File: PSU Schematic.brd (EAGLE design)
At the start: 50 x 100 mm, 19 parts, among them IC1 LM34, J1 POWERPOLE_POWER45A, J2 FUSEATC, J3 POWERPOLE_POWER45A, J4 FUSEATC

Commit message: Layout revision
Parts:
- removed U$2: SINGLE, con-lstb:SINGLE
- added CS: SINGLE, con-lstb:SINGLE
- moved IC1 2.00 mm to (14.1, 20.7)
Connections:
- net CURRENTSHARE: now also CS.1; no longer U$2.1
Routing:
- net CURRENTSHARE: track 26.0 -> 39.3 mm
- net LVCC: track 15.3 -> 18.2 mm, vias 30 -> 33
- net FAN: track 27.1 -> 29.1 mm
- net GND: track 23.1 -> 25.0 mm
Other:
- board text added: "FAN"
- board text added: "VCC"
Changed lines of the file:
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@@
 <vertex x="34.5" y="51"/>
 </polygon>
+<text x="23.5" y="29" size="1.778" layer="25" rot="R90">FAN</text>
+<text x="18" y="23" size="1.778" layer="25" rot="R270">VCC</text>
 </plain>
 <attributes>
@@
 </element>
 <element name="C2" library="resistor" package="C050-025X075" value="" x="44.09" y="81.37" rot="R270"/>
-<element name="IC1" library="linear" package="TO92" value="LM34" x="16.1" y="20.68" smashed="yes" rot="R180">
-<attribute name="NAME" x="17.687" y="24.029" size="1.27" layer="25" ratio="10" rot="R180"/>
+<element name="IC1" library="linear" package="TO92" value="LM34" x="14.1" y="20.68" smashed="yes" rot="R180">
+<attribute name="NAME" x="15.687" y="24.029" size="1.27" layer="25" ratio="10" rot="R180"/>
 </element>
 <element name="H4" library="holes" package="4,1-PAD" value="MOUNT-PAD-ROUND4.1" x="5" y="95"/>
@@
 <attribute name="NAME" x="20.428" y="23.167" size="1.27" layer="25" ratio="10"/>
 </element>
-<element name="U$2" library="con-lstb" package="SINGLE" value="SINGLE" x="13" y="20.5" smashed="yes">
-<attribute name="NAME" x="9.19" y="22.151" size="1.27" layer="25" ratio="10"/>
+<element name="CS" library="con-lstb" package="SINGLE" value="SINGLE" x="13" y="31" smashed="yes">
+<attribute name="NAME" x="9.19" y="27.651" size="1.27" layer="25" ratio="10"/>
 </element>
-<element name="R3" library="pot" package="RJ9W" value="T93YA" x="26.5" y="29.5" rot="R90"/>
+<element name="R3" library="pot" package="RJ9W" value="T93YA" x="26.5" y="29.5" smashed="yes" rot="R90">
+<attribute name="NAME" x="23.833" y="24.928" size="1.27" layer="25" ratio="10" rot="R90"/>
+</element>
 </elements>
 <signals>
@@
 <via x="16" y="48" extent="1-16" drill="0.6"/>
 <contactref element="R3" pad="E"/>
-<wire x1="23.5" y1="26.875" x2="17.375" y2="20.75" width="0.127" layer="1"/>
-<wire x1="25.75" y1="26.875" x2="23.5" y2="26.875" width="0.127" layer="1"/>
-<wire x1="17.375" y1="20.75" x2="17.37" y2="20.68" width="0.127" layer="1"/>
+<wire x1="25.75" y1="26.875" x2="23.622" y2="26.875" width="0.127" layer="1"/>
+<wire x1="23.622" y1="26.875" x2="23.5" y2="26.875" width="0.127" layer="1"/>
 <wire x1="25.75" y1="26.875" x2="25.865" y2="26.96" width="0.127" layer="1"/>
 <wire x1="30" y1="27" x2="25.875" y2="27" width="0.127" layer="1"/>
 <wire x1="25.875" y1="27" x2="25.865" y2="26.96" width="0.127" layer="1"/>
+<wire x1="15.4305" y1="22.098" x2="15.4305" y2="20.7645" width="0.127" layer="1"/>
+<wire x1="20.193" y1="26.8605" x2="15.4305" y2="22.098" width="0.127" layer="1"/>
+<wire x1="23.622" y1="26.8605" x2="20.193" y2="26.8605" width="0.127" layer="1"/>
+<wire x1="15.4305" y1="20.7645" x2="15.37" y2="20.68" width="0.127" layer="1"/>
+<wire x1="23.622" y1="26.8605" x2="23.622" y2="26.875" width="0.127" layer="1"/>
+<via x="46" y="33" extent="1-16" drill="0.6"/>
+<via x="46" y="43" extent="1-16" drill="0.6"/>
+<via x="46" y="38" extent="1-16" drill="0.6"/>
 </signal>
 <signal name="FAN">
@@
 <contactref element="U$1" pad="SIG4"/>
 <contactref element="R3" pad="S"/>
-<wire x1="21.375" y1="18.75" x2="16.125" y2="18.75" width="0.127" layer="16"/>
-<wire x1="21.375" y1="11.375" x2="21.375" y2="18.75" width="0.127" layer="16"/>
+<wire x1="21.375" y1="11.375" x2="21.375" y2="18.8595" width="0.127" layer="16"/>
+<wire x1="21.375" y1="18.8595" x2="21.375" y2="25.125" width="0.127" layer="16"/>
 <wire x1="22.5" y1="10.25" x2="21.375" y2="11.375" width="0.127" layer="16"/>
-<wire x1="16.125" y1="18.75" x2="16.1" y2="18.775" width="0.127" layer="16"/>
 <wire x1="22.5" y1="10.25" x2="22.61" y2="10.16" width="0.127" layer="16"/>
 <wire x1="21.375" y1="25.125" x2="25.75" y2="29.5" width="0.127" layer="16"/>
-<wire x1="21.375" y1="18.75" x2="21.375" y2="25.125" width="0.127" layer="16"/>
 <wire x1="25.75" y1="29.5" x2="25.865" y2="29.5" width="0.127" layer="16"/>
+<wire x1="21.375" y1="18.8595" x2="14.2875" y2="18.8595" width="0.127" layer="16"/>
+<wire x1="14.2875" y1="18.8595" x2="14.1" y2="18.775" width="0.127" layer="16"/>
 </signal>
 <signal name="GND">
@@
 <contactref element="IC1" pad="3"/>
 <contactref element="R3" pad="A"/>
-<wire x1="14.875" y1="16.5" x2="14.875" y2="20.625" width="0.127" layer="16"/>
-<wire x1="14.875" y1="20.625" x2="14.83" y2="20.68" width="0.127" layer="16"/>
-<wire x1="14.875" y1="21.125" x2="25.75" y2="32" width="0.127" layer="16"/>
-<wire x1="14.875" y1="20.75" x2="14.875" y2="21.125" width="0.127" layer="16"/>
 <wire x1="25.75" y1="32" x2="25.865" y2="32.04" width="0.127" layer="16"/>
-<wire x1="14.875" y1="20.75" x2="14.83" y2="20.68" width="0.127" layer="16"/>
+<wire x1="12.7635" y1="16.5" x2="12.7635" y2="20.574" width="0.127" layer="1"/>
+<wire x1="12.7635" y1="20.574" x2="12.83" y2="20.68" width="0.127" layer="1"/>
+<wire x1="24.1935" y1="32.004" x2="25.7175" y2="32.004" width="0.127" layer="16"/>
+<wire x1="12.954" y1="20.7645" x2="24.1935" y2="32.004" width="0.127" layer="16"/>
+<wire x1="25.7175" y1="32.004" x2="25.865" y2="32.04" width="0.127" layer="16"/>
+<wire x1="12.954" y1="20.7645" x2="12.83" y2="20.68" width="0.127" layer="16"/>
 </signal>
 <signal name="CURRENTSHARE">
 <contactref element="U$1" pad="SIG11"/>
-<contactref element="U$2" pad="1"/>
-<wire x1="13.875" y1="17.125" x2="10.5" y2="20.5" width="0.127" layer="1"/>
-<wire x1="20.375" y1="17.125" x2="13.875" y2="17.125" width="0.127" layer="1"/>
-<wire x1="24" y1="13.5" x2="20.375" y2="17.125" width="0.127" layer="1"/>
-<wire x1="24" y1="5.125" x2="24" y2="13.5" width="0.127" layer="1"/>
-<wire x1="25.125" y1="5.125" x2="24" y2="5.125" width="0.127" layer="1"/>
-<wire x1="10.5" y1="20.5" x2="10.46" y2="20.5" width="0.127" layer="1"/>
-<wire x1="25.125" y1="5.125" x2="25.15" y2="5.08" width="0.127" layer="1"/>
-</signal>
-<signal name="LVCC1">
-<via x="46" y="33" extent="1-16" drill="0.6"/>
-<via x="46" y="43" extent="1-16" drill="0.6"/>
-<via x="46" y="38" extent="1-16" drill="0.6"/>
+<contactref element="CS" pad="1"/>
+<wire x1="10.4775" y1="20.955" x2="10.4775" y2="30.861" width="0.127" layer="16"/>
+<wire x1="14.2875" y1="17.145" x2="10.4775" y2="20.955" width="0.127" layer="16"/>
+<wire x1="20.193" y1="17.145" x2="14.2875" y2="17.145" width="0.127" layer="16"/>
+<wire x1="20.955" y1="16.383" x2="20.193" y2="17.145" width="0.127" layer="16"/>
+<wire x1="20.955" y1="4.572" x2="20.955" y2="16.383" width="0.127" layer="16"/>
+<wire x1="21.717" y1="3.81" x2="20.955" y2="4.572" width="0.127" layer="16"/>
+<wire x1="24.003" y1="3.81" x2="21.717" y2="3.81" width="0.127" layer="16"/>
+<wire x1="25.146" y1="4.953" x2="24.003" y2="3.81" width="0.127" layer="16"/>
+<wire x1="10.4775" y1="30.861" x2="10.46" y2="31" width="0.127" layer="16"/>
+<wire x1="25.146" y1="4.953" x2="25.15" y2="5.08" width="0.127" layer="16"/>
 </signal>
 </signals>

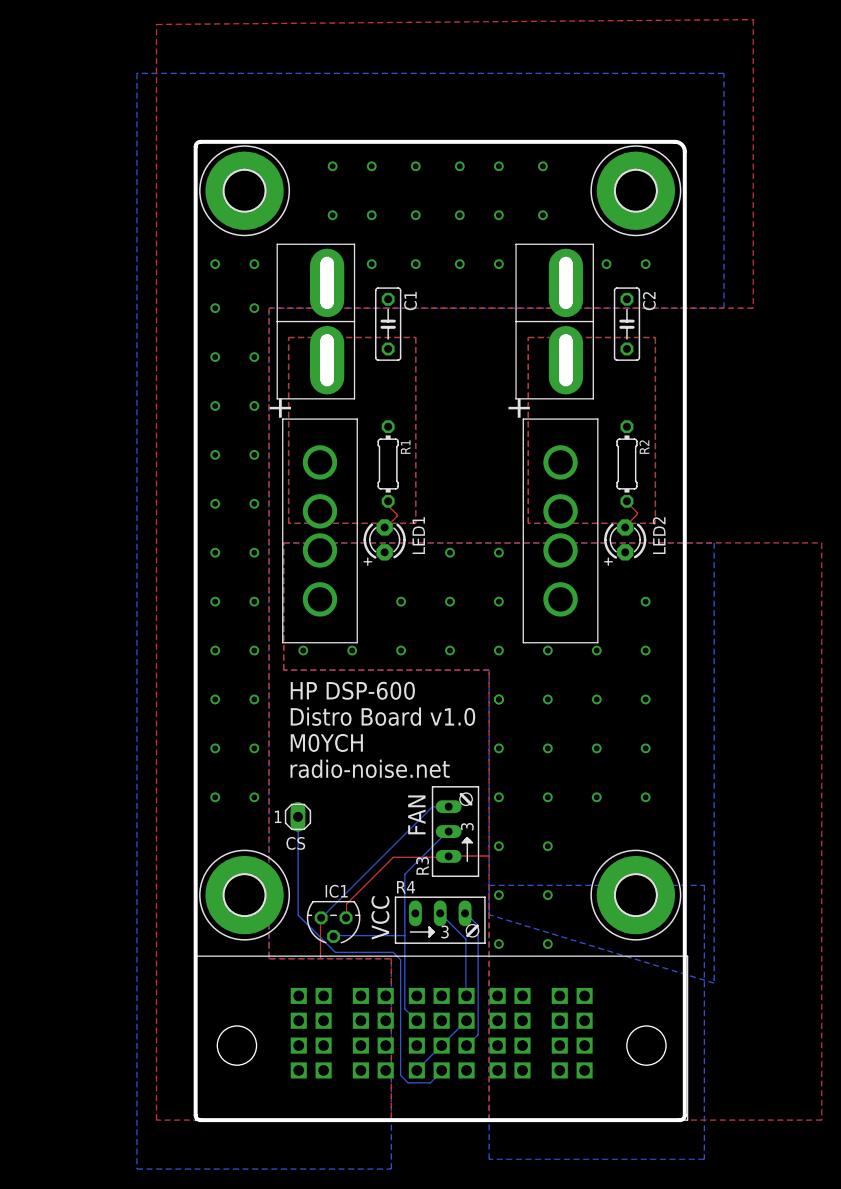
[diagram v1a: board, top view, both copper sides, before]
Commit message: Corrected layout
Flipped design to correct mis-match which would have occured.
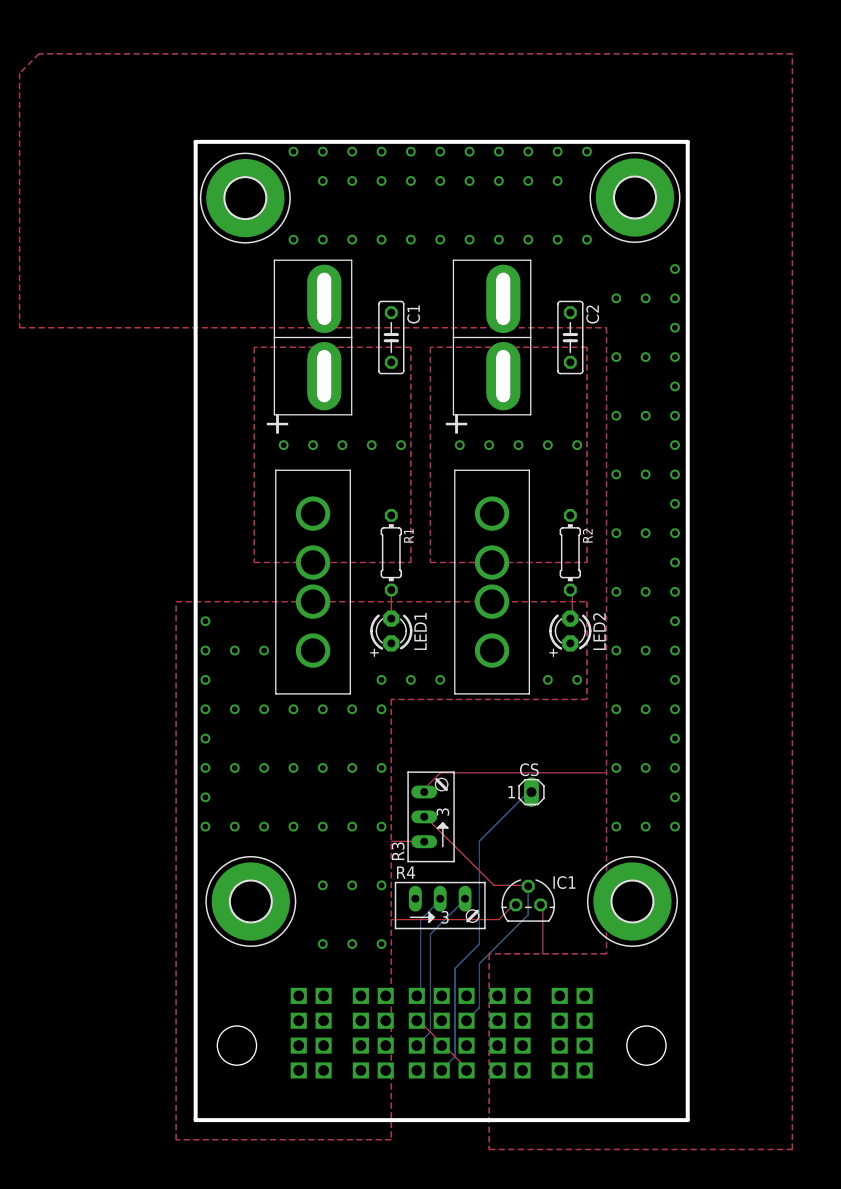
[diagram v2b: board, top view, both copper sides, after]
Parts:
- U$2: value 51730-073LF -> 51760-10201202AALF51760-10201202AALF
- moved H4 82.8 mm to (44.6, 22.4)
- moved H2 81.7 mm to (44.9, 94.3)
- moved H1 39.9 mm to (5.08, 94.2)
- moved H3 39.4 mm to (5.64, 22.4)
- moved CS 24.0 mm to (36.9, 33.5)
- moved IC1 19.9 mm to (34.0, 22.0), turned to 0 degrees
- moved LED2 10.9 mm to (38.3, 50.0)
- moved R2 10.8 mm to (38.3, 58.0)
- moved LED1 9.33 mm to (20.0, 50.0)
- moved R1 9.08 mm to (20.0, 58.0)
- moved J4 8.74 mm to (30.3, 55.0)
- moved J3 6.60 mm to (30.3, 80.0)
- moved C2 5.95 mm to (38.3, 80.0)
- moved J2 5.28 mm to (12.0, 55.0)
- moved R3 2.92 mm to (24.0, 31.0)
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- renumbered U$1 to U$2
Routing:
- net CURRENTSHARE: track 39.3 -> 32.4 mm
- net VCTRL: track 14.6 -> 17.0 mm
- net LVCC: track 18.2 -> 16.7 mm, vias 33 -> 39
- net 5VCC: track 9.55 -> 11.0 mm
- net FAN: track 29.1 -> 30.0 mm
- net N$4: track 3.70 -> 2.92 mm
- net N$5: track 3.66 -> 3.08 mm
- net GND: track 25.0 -> 24.8 mm, vias 42 -> 71
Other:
- board size 50 x 100 mm -> 50.3 x 100 mm
- board text removed: "FAN"
- board text removed: "HP DSP-600 Distro Board v1.0 M0YCH radio-noise.net"
- board text removed: "VCC"

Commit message: bStop Added
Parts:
- moved CS 6.00 mm to (36.9, 27.5)
- moved H2 0.79 mm to (45.3, 95.0)
- moved H1 0.75 mm to (5.00, 95.0)
- moved H4 0.74 mm to (45.3, 22.0)
- moved H3 0.73 mm to (5.00, 22.0)
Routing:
- net CURRENTSHARE: track 32.4 -> 28.2 mm
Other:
- outline, holes or cut-outs redrawn
- board text added: "HP DPS-600 Distribution M0YCH"
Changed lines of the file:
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@@
 <layer number="28" name="bValues" color="7" fill="1" visible="yes" active="yes"/>
 <layer number="29" name="tStop" color="7" fill="3" visible="no" active="yes"/>
-<layer number="30" name="bStop" color="7" fill="6" visible="no" active="yes"/>
+<layer number="30" name="bStop" color="7" fill="6" visible="yes" active="yes"/>
 <layer number="31" name="tCream" color="7" fill="4" visible="no" active="yes"/>
 <layer number="32" name="bCream" color="7" fill="5" visible="no" active="yes"/>
@@
 <board>
 <plain>
+<wire x1="50.3" y1="0" x2="50.3" y2="96.087553125" width="0.4064" layer="20"/>
+<wire x1="50.3" y1="96.087553125" x2="46.387553125" y2="100" width="0.4064" layer="20" curve="90"/>
+<wire x1="46.387553125" y1="100" x2="3.41420625" y2="100" width="0.4064" layer="20"/>
+<wire x1="3.41420625" y1="100" x2="0" y2="96.58579375" width="0.4064" layer="20" curve="90"/>
+<wire x1="0" y1="96.58579375" x2="0" y2="0" width="0.4064" layer="20"/>
 <wire x1="0" y1="0" x2="50.3" y2="0" width="0.4064" layer="20"/>
-<wire x1="50.3" y1="0" x2="50.3" y2="100" width="0.4064" layer="20"/>
-<wire x1="50.3" y1="100" x2="0" y2="100" width="0.4064" layer="20"/>
-<wire x1="0" y1="100" x2="0" y2="0" width="0.4064" layer="20"/>
+<text x="41" y="35" size="1.778" layer="25" align="bottom-right">HP DPS-600
+Distribution
+M0YCH</text>
+<polygon width="0.4064" layer="30">
+<vertex x="30" y="14"/>
+<vertex x="41" y="14"/>
+<vertex x="41" y="4"/>
+<vertex x="30" y="4"/>
+</polygon>
+<polygon width="0.4064" layer="30">
+<vertex x="10" y="4"/>
+<vertex x="20" y="4"/>
+<vertex x="20" y="14"/>
+<vertex x="9" y="14"/>
+<vertex x="9" y="4"/>
+</polygon>
+<polygon width="0.4064" layer="30">
+<vertex x="9" y="53"/>
+<vertex x="9" y="45"/>
+<vertex x="15" y="45"/>
+<vertex x="15" y="53"/>
+</polygon>
+<polygon width="0.4064" layer="30">
+<vertex x="27" y="53"/>
+<vertex x="27" y="45"/>
+<vertex x="33" y="45"/>
+<vertex x="33" y="53"/>
+</polygon>
+<polygon width="0.4064" layer="30">
+<vertex x="9" y="78"/>
+<vertex x="9" y="57"/>
+<vertex x="15" y="57"/>
+<vertex x="15" y="79"/>
+<vertex x="9" y="79"/>
+</polygon>
+<polygon width="0.4064" layer="30">
+<vertex x="27" y="57"/>
+<vertex x="27" y="79"/>
+<vertex x="33" y="79"/>
+<vertex x="33" y="57"/>
+</polygon>
+<polygon width="0.4064" layer="30">
+<vertex x="10" y="88"/>
+<vertex x="10" y="81"/>
+<vertex x="39" y="81"/>
+<vertex x="39" y="88"/>
+</polygon>
 </plain>
 <attributes>
@@
 <element name="C2" library="resistor" package="C050-025X075" value="" x="38.3" y="80" rot="R270"/>
 <element name="IC1" library="linear" package="TO92" value="LM34" x="34" y="22" smashed="yes">
-<attribute name="NAME" x="36.413" y="23.651" size="1.27" layer="25" ratio="10"/>
+<attribute name="NAME" x="33.413" y="18.651" size="1.27" layer="25" ratio="10"/>
 </element>
-<element name="H4" library="holes" package="4,1-PAD" value="MOUNT-PAD-ROUND4.1" x="44.65" y="22.35"/>
-<element name="H1" library="holes" package="4,1-PAD" value="MOUNT-PAD-ROUND4.1" x="5.08" y="94.25"/>
-<element name="H2" library="holes" package="4,1-PAD" value="MOUNT-PAD-ROUND4.1" x="44.91" y="94.31"/>
-<element name="H3" library="holes" package="4,1-PAD" value="MOUNT-PAD-ROUND4.1" x="5.64" y="22.35"/>
+<element name="H4" library="holes" package="4,1-PAD" value="MOUNT-PAD-ROUND4.1" x="45.3" y="22"/>
+<element name="H1" library="holes" package="4,1-PAD" value="MOUNT-PAD-ROUND4.1" x="5" y="95"/>
+<element name="H2" library="holes" package="4,1-PAD" value="MOUNT-PAD-ROUND4.1" x="45.3" y="95"/>
+<element name="H3" library="holes" package="4,1-PAD" value="MOUNT-PAD-ROUND4.1" x="5" y="22"/>
 <element name="R4" library="pot" package="RJ9W" value="T93YA" x="25" y="22" smashed="yes">
 <attribute name="NAME" x="20.428" y="24.667" size="1.27" layer="25" ratio="10"/>
 </element>
-<element name="CS" library="con-lstb" package="SINGLE" value="SINGLE" x="36.87" y="33.53" smashed="yes">
-<attribute name="NAME" x="33.06" y="35.181" size="1.27" layer="25" ratio="10"/>
+<element name="CS" library="con-lstb" package="SINGLE" value="SINGLE" x="36.87" y="27.53" smashed="yes">
+<attribute name="NAME" x="33.06" y="29.181" size="1.27" layer="25" ratio="10"/>
 </element>
 <element name="R3" library="pot" package="RJ9W" value="T93YA" x="24" y="31" smashed="yes" rot="R90">
@@
 <contactref element="CS" pad="1"/>
 <contactref element="U$2" pad="SIG11"/>
-<wire x1="29" y1="28.5" x2="34" y2="33.5" width="0.127" layer="16"/>
-<wire x1="29" y1="18" x2="29" y2="28.5" width="0.127" layer="16"/>
+<wire x1="29" y1="25.5" x2="31" y2="27.5" width="0.127" layer="16"/>
+<wire x1="29" y1="18" x2="29" y2="25.5" width="0.127" layer="16"/>
 <wire x1="26.5" y1="15.5" x2="29" y2="18" width="0.127" layer="16"/>
 <wire x1="26.5" y1="6.5" x2="26.5" y2="15.5" width="0.127" layer="16"/>
 <wire x1="25.5" y1="5.5" x2="26.5" y2="6.5" width="0.127" layer="16"/>
-<wire x1="34" y1="33.5" x2="34.33" y2="33.53" width="0.127" layer="16"/>
+<wire x1="31" y1="27.5" x2="34.33" y2="27.53" width="0.127" layer="16"/>
 <wire x1="25.5" y1="5.5" x2="25.15" y2="5.08" width="0.127" layer="16"/>
 </signal>
@@
 </board>
 </drawing>
+<compatibility>
+<note version="6.3" minversion="6.2.2" severity="warning">
+Since Version 6.2.2 text objects can contain more than one line,
+which will not be processed correctly with this version.
+</note>
+</compatibility>
 </eagle>
